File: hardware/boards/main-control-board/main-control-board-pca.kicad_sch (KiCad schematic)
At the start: 1 part

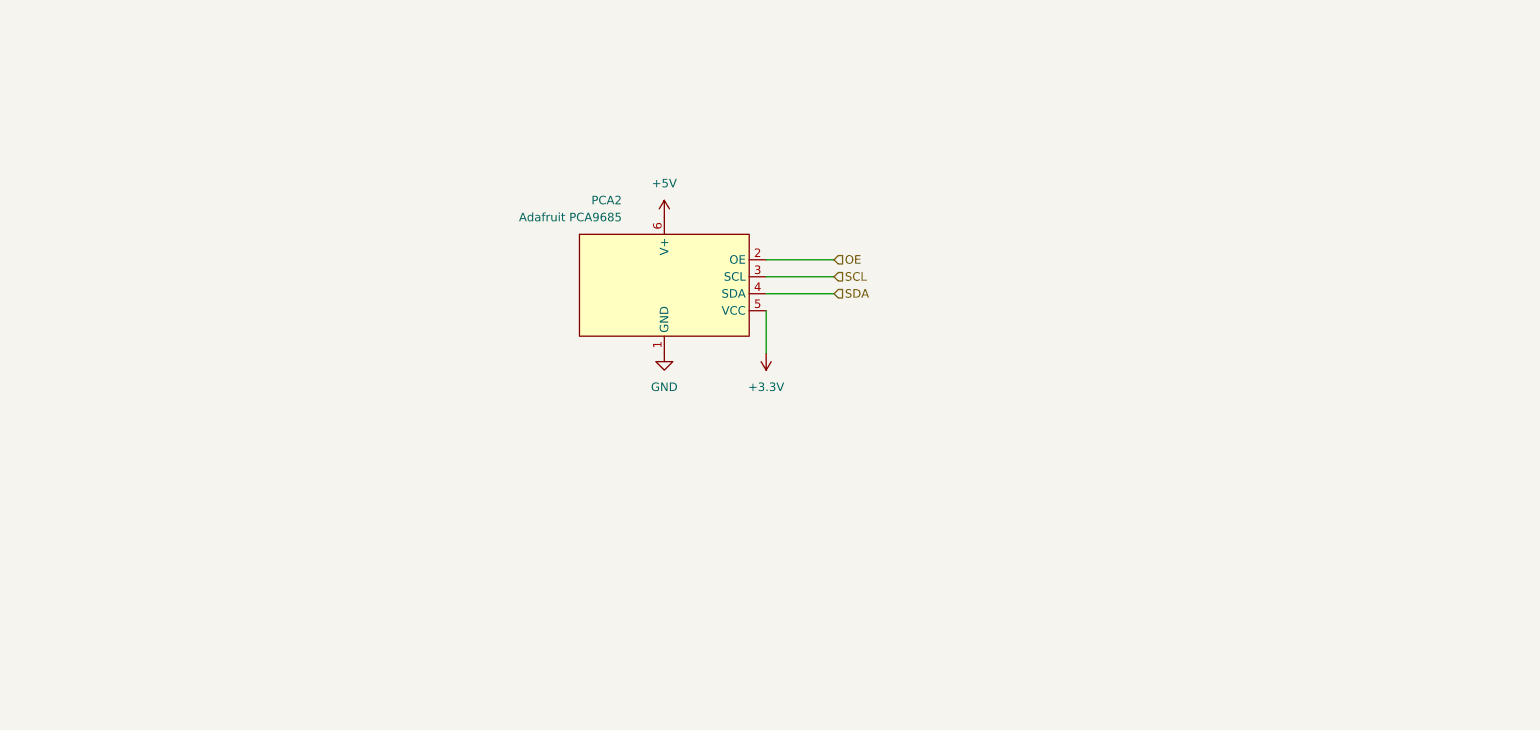
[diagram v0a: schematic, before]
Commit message: integrate PCA into the board
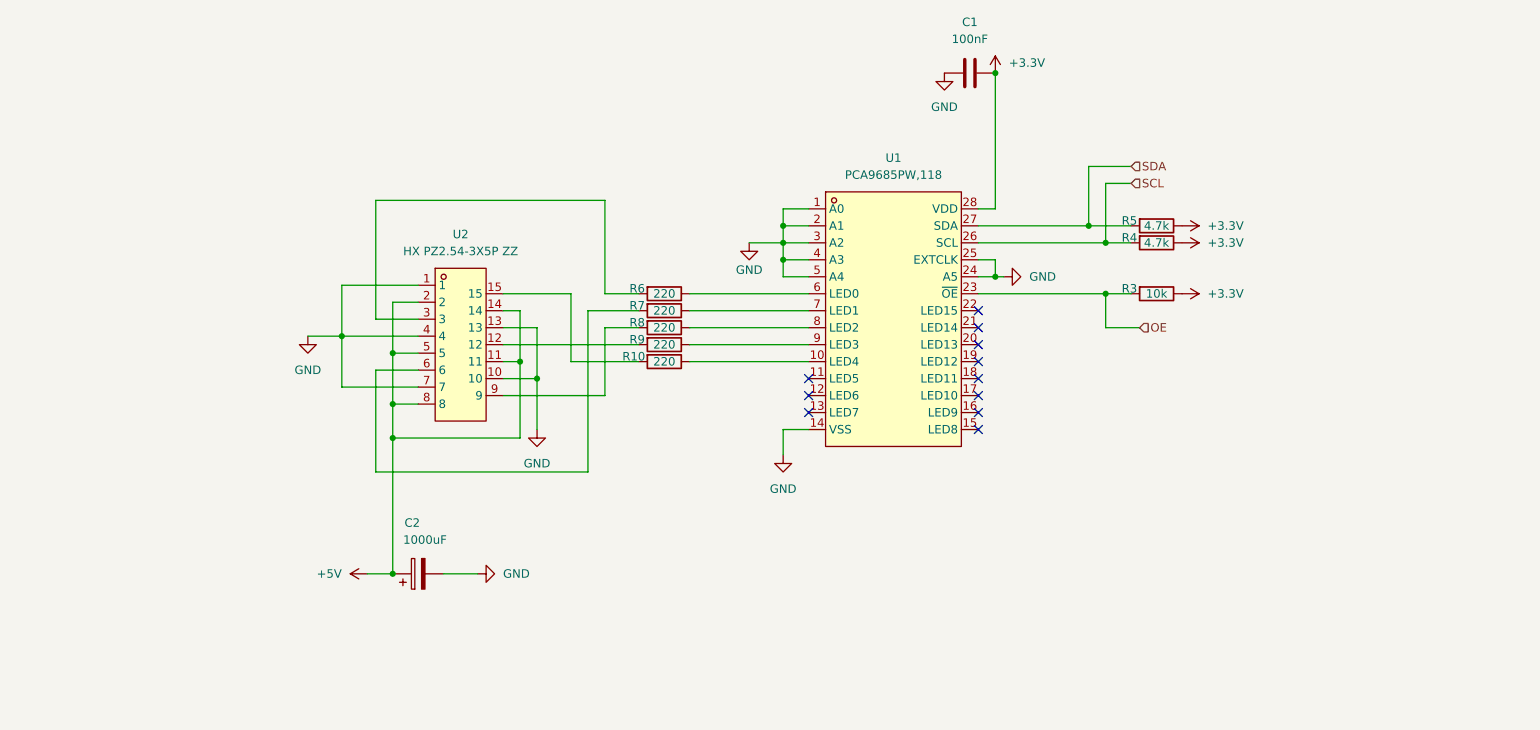
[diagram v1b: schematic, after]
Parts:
- removed PCA2: Adafruit PCA9685, symbol TinyEngineerModules:Adafruit_PCA9685_Module
- added C1: 100nF, Capacitor_SMD:C_0603_1608Metric, symbol Device:C
- added C2: 1000uF, Capacitor_SMD:CP_Elec_10x10.5, symbol Device:C_Polarized
- added R10, R6, R7, R8, R9: 220, Resistor_SMD:R_0603_1608Metric, symbol Device:R
- added R3: 10k, Resistor_SMD:R_0603_1608Metric, symbol Device:R
- added R4, R5: 4.7k, Resistor_SMD:R_0603_1608Metric, symbol Device:R
- added U1: PCA9685PW,118, easyeda:TSSOP-28_L9.7-W4.4-P0.65-LS6.4-TL, symbol easyeda:PCA9685PW,118
- added U2: HX PZ2.54-3X5P ZZ, easyeda:HDR-TH_15P-P2.54-V-M-R3-C5-S7.5, symbol easyeda:HXPZ2.54-3X5PZZ
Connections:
- net +3.3V: now also C1.2, R3.1, R4.1, R5.1, U1.28 (VDD)
- net +5V: now also C2.1, U2.11, U2.14, U2.2, U2.5, U2.8
- net GND: now also C1.1, C2.2, U1.1 (A0), U1.14 (VSS), U1.2 (A1), U1.24 (A5), U1.25 (EXTCLK), U1.3 (A2), U1.4 (A3), U1.5 (A4), U2.1, U2.10, U2.13, U2.4, U2.7
- net OE: now also R3.2, U1.23 (~{OE})
- net SCL: now also R4.2, U1.26 (SCL)
- net SDA: now also R5.2, U1.27 (SDA)
- new net: R10.1, U1.10 (LED4)
- new net: R10.2, U2.15
- new net: R8.1, U1.8 (LED2)
- new net: R8.2, U2.9
- new net: R6.1, U1.6 (LED0)
- new net: R7.1, U1.7 (LED1)
- new net: R9.1, U1.9 (LED3)
- new net: R6.2, U2.3
- new net: R9.2, U2.12
- new net: R7.2, U2.6
- no-connect marks 0 -> 11

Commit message: set FT Rotation Offset to fix JLCPCB orientation
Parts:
- C2: FT Rotation Offset (none) -> 180
- U1: FT Rotation Offset (none) -> 90
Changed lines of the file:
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@@
+			)
+		)
+		(property "FT Rotation Offset" "90"
+			(at 166.37 91.44 0)
+			(hide yes)
+			(show_name no)
+			(do_not_autoplace no)
+			(effects
+				(font
+					(size 1.27 1.27)
+				)
 			)
 		)
@@
 			(at 95.25 129.54 90)
 			(hide yes)
+			(show_name no)
+			(do_not_autoplace no)
+			(effects
+				(font
+					(size 1.27 1.27)
+				)
+			)
+		)
+		(property "FT Rotation Offset" "180"
+			(at 95.25 129.54 90)
+			(hide yes)

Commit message: use basic components over extended
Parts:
- C1: LCSC Part # C1590 -> C14663
- R10, R6, R7, R8, R9: LCSC Part # C2907127 -> C22962
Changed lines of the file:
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@@
 			)
 		)
-		(property "LCSC Part #" "C2907127"
+		(property "LCSC Part #" "C22962"
 			(at 132.08 97.79 90)
 			(hide yes)
@@
 			)
 		)
-		(property "LCSC Part #" "C2907127"
+		(property "LCSC Part #" "C22962"
 			(at 132.08 92.71 90)
 			(hide yes)
@@
 			)
 		)
-		(property "LCSC Part #" "C1590"
+		(property "LCSC Part #" "C14663"
 			(at 177.8 54.61 90)
 			(hide yes)
@@
 			)
 		)
-		(property "LCSC Part #" "C2907127"
+		(property "LCSC Part #" "C22962"
 			(at 132.08 87.63 90)
 			(hide yes)
@@
 			)
 		)
-		(property "LCSC Part #" "C2907127"
+		(property "LCSC Part #" "C22962"
 			(at 132.08 95.25 90)
 			(hide yes)
@@
 			)
 		)
-		(property "LCSC Part #" "C2907127"
+		(property "LCSC Part #" "C22962"
 			(at 132.08 90.17 90)
 			(hide yes)

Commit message: pre-fab improvements
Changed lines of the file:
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@@
 	)
 	(hierarchical_label "SCL"
-		(shape input)
+		(shape bidirectional)
 		(at 201.93 71.12 0)
 		(effects
@@
 	)
 	(hierarchical_label "SDA"
-		(shape input)
+		(shape bidirectional)
 		(at 201.93 68.58 0)
 		(effects

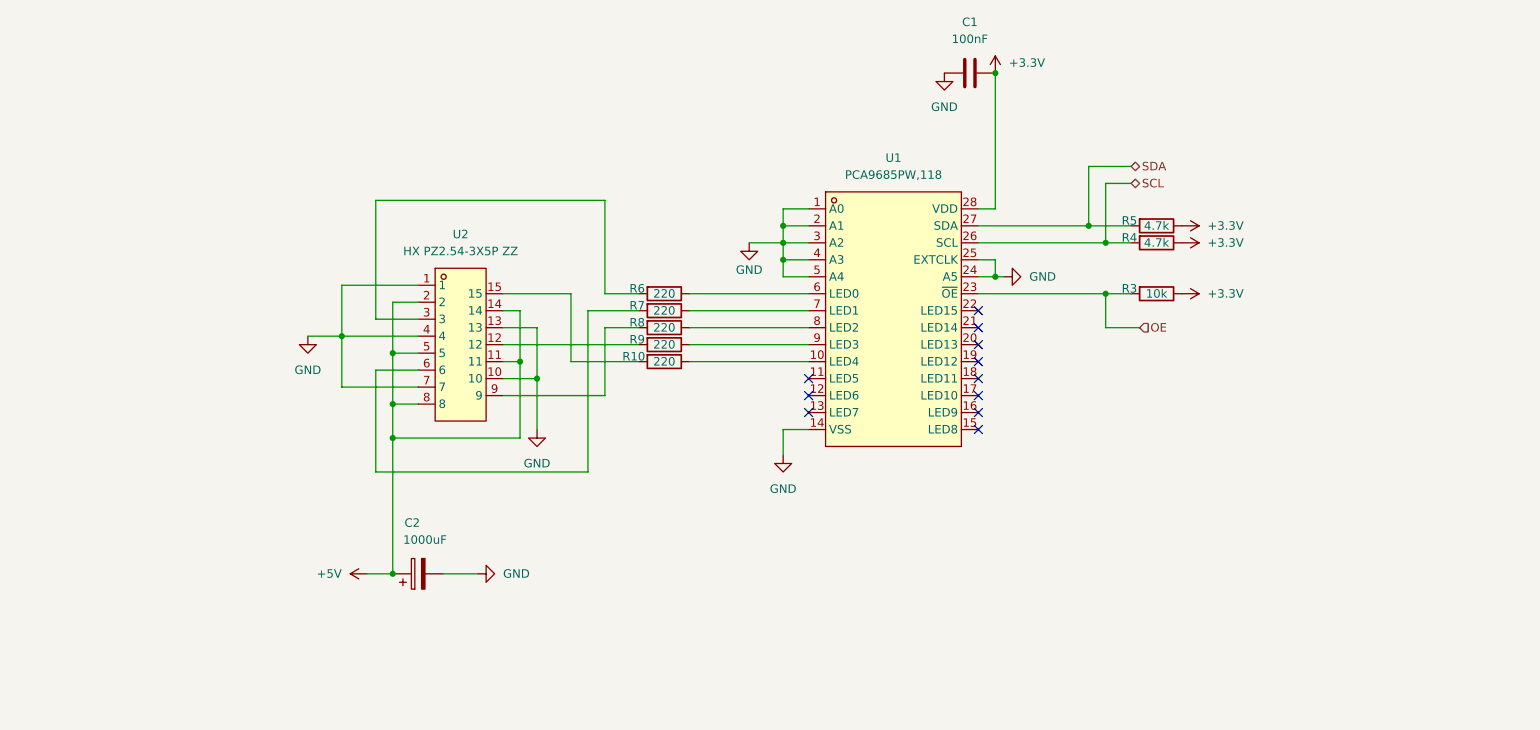
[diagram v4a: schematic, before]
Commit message: add efuse before 5V servo rail
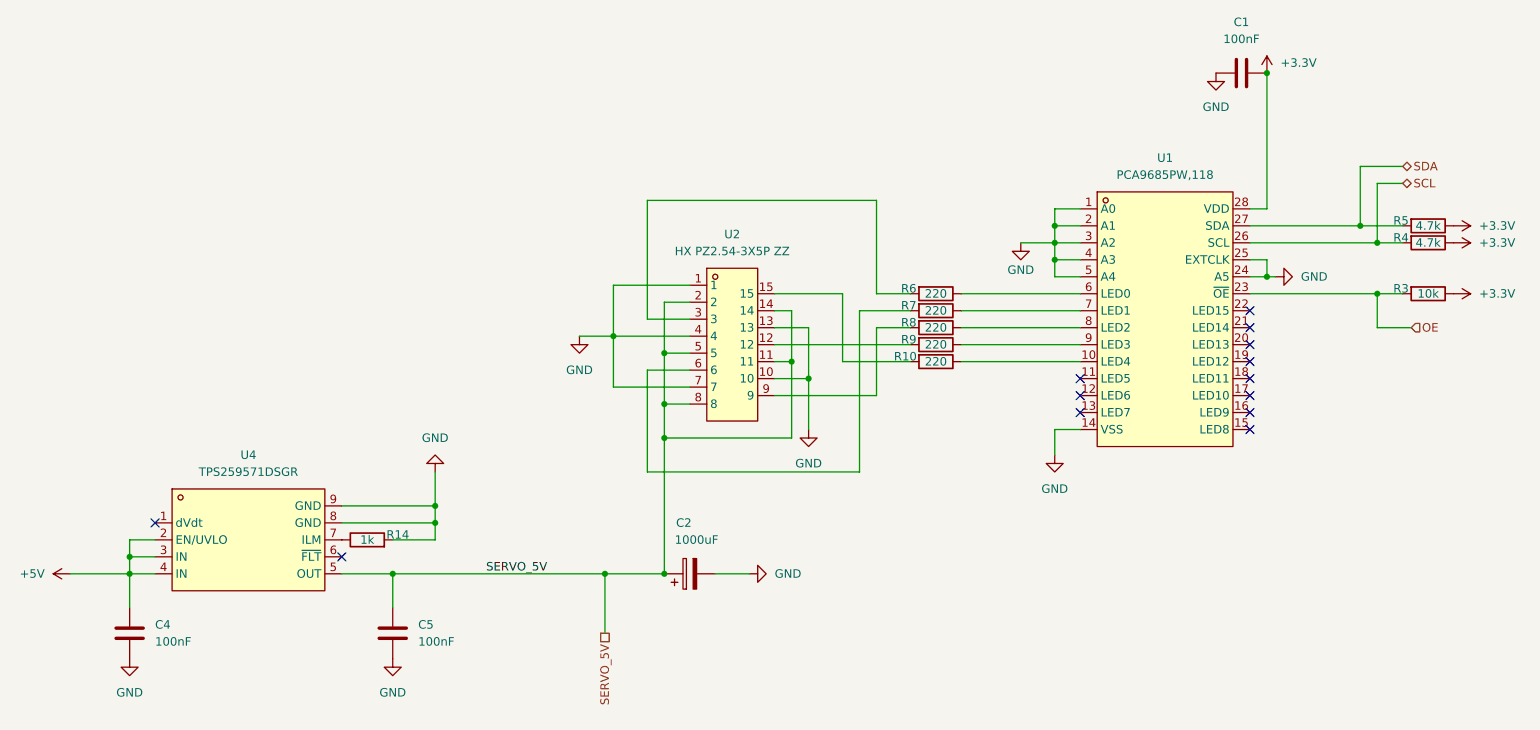
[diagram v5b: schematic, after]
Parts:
- added C4, C5: 100nF, Capacitor_SMD:C_0603_1608Metric, symbol Device:C
- added R14: 1k, Resistor_SMD:R_0603_1608Metric, symbol Device:R
- added U4: TPS259571DSGR, easyeda:WSON-8_L2.0-W2.0-P0.50-TL-EP, symbol easyeda:TPS259571DSGR
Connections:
- net +5V: now also C4.2, U4.2 (EN/UVLO), U4.3 (IN), U4.4 (IN); no longer C2.1, U2.11, U2.14, U2.2, U2.5, U2.8
- net GND: now also C4.1, C5.1, R14.2, U4.8 (GND), U4.9 (GND)
- new net: R14.1, U4.7 (ILM)
- new net SERVO_5V: C2.1, C5.2, U2.11, U2.14, U2.2, U2.5, U2.8, U4.5 (OUT)
- no-connect marks 11 -> 13
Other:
- moved on the sheet: C1, C2, R10, R3, R4, R5, R6, R7, R8, R9, U1, U2

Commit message: feat(pcb): update component properties and add missing attributes
- Renamed connection values for ESP32 components to standardize naming.
- Added properties for KiLib_Generator, MPN, and Manufacturer for various components across multiple schematic files.
- Enhanced documentation for component attributes to improve clarity and accessibility in the design process.
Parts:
- C1, C4, C5: MPN (none) -> CC0603KRX7R9BB104; Manufacturer (none) -> YAGEO
- C2: MPN (none) -> JVJ16V1000M10x10; Manufacturer (none) -> jieerrui
- R10, R6, R7, R8, R9: MPN (none) -> 0603WAF2200T5E; Manufacturer (none) -> UNI-ROYAL(Uniroyal Elec)
- R14: MPN (none) -> 0603WAF1001T5E; Manufacturer (none) -> UNI-ROYAL(Uniroyal Elec)
- R3: MPN (none) -> 0603WAF1002T5E; Manufacturer (none) -> UNI-ROYAL(Uniroyal Elec)
- R4, R5: MPN (none) -> 0603WAF4701T5E; Manufacturer (none) -> UNI-ROYAL(Uniroyal Elec)
- U1: Manufacturer NXP(恩智浦) -> NXP Semicon
- U2: Manufacturer hanxia(韩下) -> hanxia
- U4: Manufacturer TI(德州仪器) -> Texas Instruments
